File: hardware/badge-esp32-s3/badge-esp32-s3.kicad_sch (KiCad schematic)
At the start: 4 parts, among them U4 ESP32-S3-MINI-1-N8

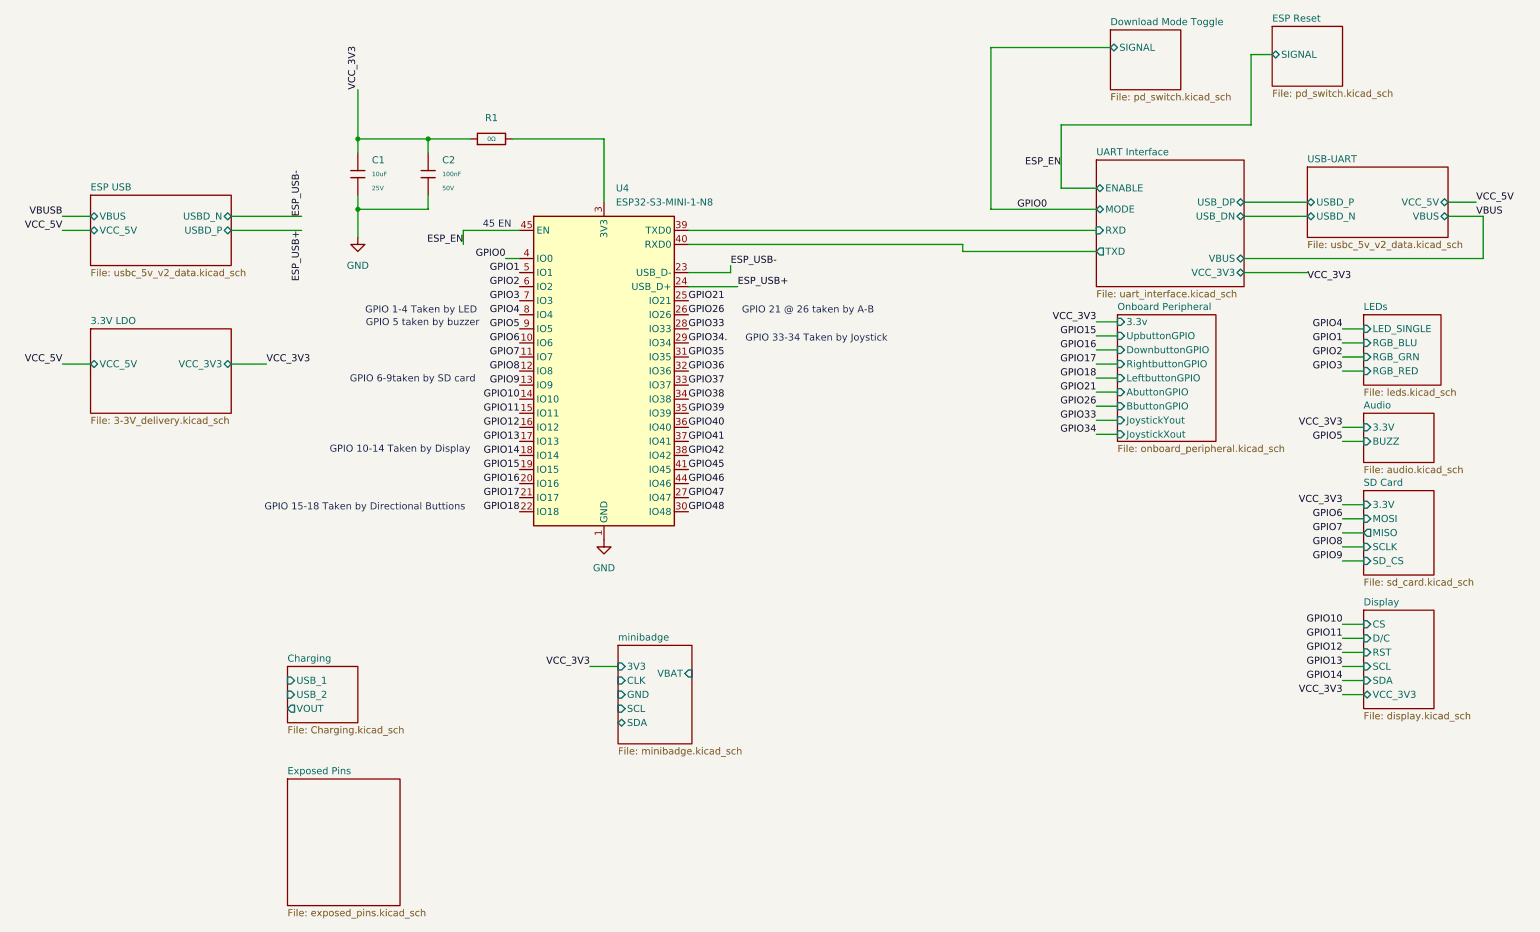
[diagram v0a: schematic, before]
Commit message: Fleshed out schematic with all exposed pins
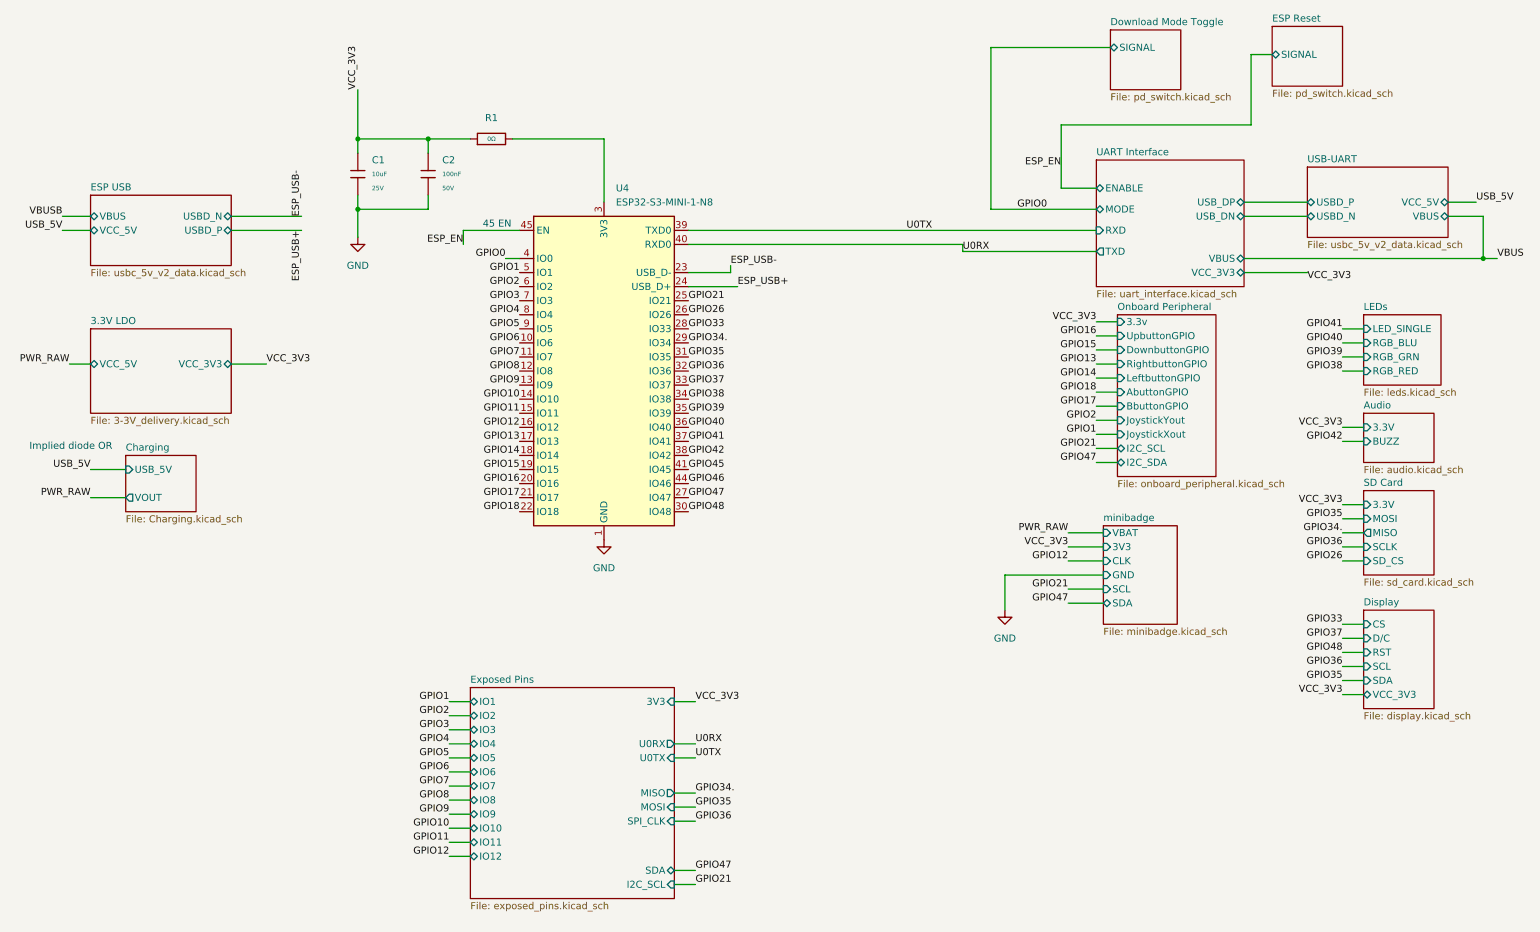
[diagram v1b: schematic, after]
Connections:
- net UART Interface/RXD renamed U0TX
- net UART Interface/TXD renamed U0RX
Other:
- sheet Charging ports: added USB_5V; removed USB_1, USB_2
- sheet Exposed Pins ports: added 3V3, I2C_SCL, IO1, IO10, IO11, IO12, IO2, IO3, IO4, IO5, IO6, IO7, IO8, IO9, MISO, MOSI, SDA, SPI_CLK, U0RX, U0TX; removed none
- sheet Onboard Peripheral ports: added I2C_SCL, I2C_SDA; removed none
- note added: "Implied diode OR"
- note removed: "GPIO 1-4 Taken by LED"
- note removed: "GPIO 10-14 Taken by Display"
- note removed: "GPIO 15-18 Taken by Directional Buttions"
- note removed: "GPIO 21 @ 26 taken by A-B"
- note removed: "GPIO 33-34 Taken by Joystick"
- note removed: "GPIO 5 taken by buzzer"
- note removed: "GPIO 6-9taken by SD card"

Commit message: Annotate schematic
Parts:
- renumbered U4 to U1
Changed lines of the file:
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@@
 		(dnp no)
 		(fields_autoplaced yes)
-		(property "Reference" "#PWR031"
+		(property "Reference" "#PWR02"
 			(at 118.11 114.3 0)
 			(effects
@@
 			(project ""
 				(path "/e2af9a6c-dbe9-4de2-9ba6-ea213a7300ec"
-					(reference "#PWR031")
+					(reference "#PWR02")
 					(unit 1)
 				)
@@
 		(dnp no)
 		(fields_autoplaced yes)
-		(property "Reference" "U4"
+		(property "Reference" "U1"
 			(at 120.2533 44.45 0)
 			(effects
@@
 			(project ""
 				(path "/e2af9a6c-dbe9-4de2-9ba6-ea213a7300ec"
-					(reference "U4")
+					(reference "U1")
 					(unit 1)
 				)
@@
 		(dnp no)
 		(fields_autoplaced yes)
-		(property "Reference" "#PWR047"
+		(property "Reference" "#PWR03"
 			(at 190.5 127 0)
 			(effects
@@
 			(project ""
 				(path "/e2af9a6c-dbe9-4de2-9ba6-ea213a7300ec"
-					(reference "#PWR047")
+					(reference "#PWR03")
 					(unit 1)
 				)
@@
 		(dnp no)
 		(fields_autoplaced yes)
-		(property "Reference" "#PWR021"
+		(property "Reference" "#PWR01"
 			(at 73.66 59.69 0)
 			(effects
@@
 			(project "badge-esp32-s3"
 				(path "/e2af9a6c-dbe9-4de2-9ba6-ea213a7300ec"
-					(reference "#PWR021")
+					(reference "#PWR01")
 					(unit 1)
 				)

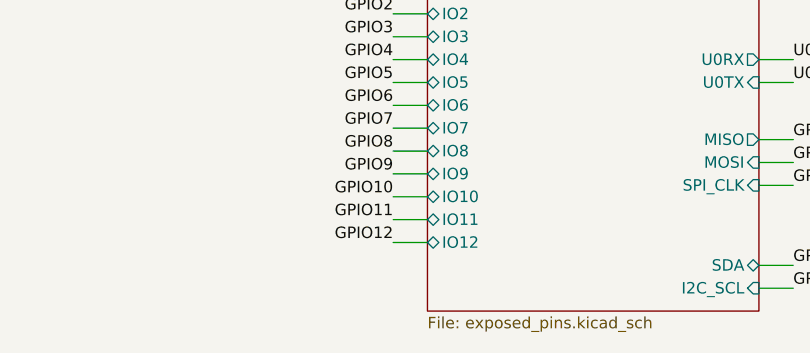
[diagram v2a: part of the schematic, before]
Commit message: Fix some DRC errors
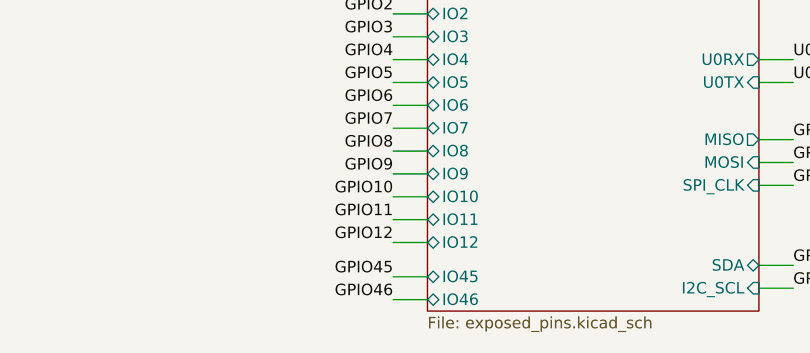
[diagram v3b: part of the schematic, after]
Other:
- sheet Exposed Pins ports: added IO45, IO46; removed none
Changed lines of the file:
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@@
+	(wire
+		(pts
+			(xy 90.17 168.91) (xy 93.98 168.91)
+		)
+		(stroke
+			(width 0)
+			(type default)
+		)
+	)
 	(wire
 		(pts
@@
 		(pts
 			(xy 238.76 20.32) (xy 234.95 20.32)
+		)
+		(stroke
+			(width 0)
+			(type default)
+		)
+	)
+	(wire
+		(pts
+			(xy 90.17 171.45) (xy 93.98 171.45)
 		)
 		(stroke
@@
 		)
 	)
+	(label "GPIO45"
+		(at 90.17 168.91 180)
+		(effects
+			(font
+				(size 1.27 1.27)
+			)
+			(justify right bottom)
+		)
+	)
 	(label "VCC_3V3"
 		(at 251.46 87.63 180)
@@
 	(label "GPIO6"
 		(at 102.87 72.39 180)
+		(effects
+			(font
+				(size 1.27 1.27)
+			)
+			(justify right bottom)
+		)
+	)
+	(label "GPIO46"
+		(at 90.17 171.45 180)
 		(effects
 			(font
@@
 			(effects
 				(font
+					(size 1.27 1.27)
+				)
+				(justify left)
+			)
+		)
+		(pin "IO45" bidirectional
+			(at 93.98 168.91 180)
+			(effects
+				(font
+					(size 1.27 1.27)
+				)
+				(justify left)
+			)
+		)
+		(pin "IO46" bidirectional
+			(at 93.98 171.45 180)
+			(effects
+				(font

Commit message: Finish schematic, start placing parts on layout
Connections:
- net VCC_3V3 renamed +3.3V
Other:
- sheet minibadge ports: added none; removed GND
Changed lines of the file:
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@@
 	)
 	(junction
+		(at 54.61 76.2)
+		(diameter 0)
+		(color 0 0 0 0)
+	)
+	(junction
 		(at 276.86 57.15)
 		(diameter 0)
@@
 	)
 	(junction
+		(at 26.67 100.33)
+		(diameter 0)
+		(color 0 0 0 0)
+	)
+	(junction
 		(at 73.66 48.26)
 		(diameter 0)
@@
 	(wire
 		(pts
+			(xy 26.67 109.22) (xy 26.67 100.33)
+		)
+		(stroke
+			(width 0)
+			(type default)
+		)
+	)
+	(wire
+		(pts
 			(xy 201.93 106.68) (xy 208.28 106.68)
 		)
@@
 	(wire
 		(pts
+			(xy 26.67 100.33) (xy 31.75 100.33)
+		)
+		(stroke
+			(width 0)
+			(type default)
+		)
+	)
+	(wire
+		(pts
 			(xy 251.46 109.22) (xy 255.27 109.22)
 		)
@@
 	(wire
 		(pts
-			(xy 73.66 48.26) (xy 73.66 53.34)
+			(xy 54.61 76.2) (xy 57.15 76.2)
 		)
 		(stroke
@@
 	(wire
 		(pts
-			(xy 251.46 74.93) (xy 255.27 74.93)
+			(xy 73.66 48.26) (xy 73.66 53.34)
 		)
 		(stroke
@@
 	(wire
 		(pts
-			(xy 190.5 114.3) (xy 190.5 120.65)
+			(xy 251.46 74.93) (xy 255.27 74.93)
 		)
 		(stroke
@@
 	(wire
 		(pts
-			(xy 86.36 35.56) (xy 86.36 38.1)
+			(xy 54.61 73.66) (xy 54.61 76.2)
 		)
 		(stroke
@@
 	(wire
 		(pts
-			(xy 90.17 147.32) (xy 93.98 147.32)
+			(xy 86.36 35.56) (xy 86.36 38.1)
 		)
 		(stroke
@@
 	(wire
 		(pts
-			(xy 90.17 154.94) (xy 93.98 154.94)
+			(xy 90.17 147.32) (xy 93.98 147.32)
 		)
 		(stroke
@@
 	(wire
 		(pts
-			(xy 73.66 35.56) (xy 73.66 38.1)
+			(xy 90.17 154.94) (xy 93.98 154.94)
 		)
 		(stroke
@@
 	(wire
 		(pts
-			(xy 251.46 90.17) (xy 255.27 90.17)
+			(xy 73.66 35.56) (xy 73.66 38.1)
 		)
 		(stroke
@@
 	(wire
 		(pts
-			(xy 208.28 114.3) (xy 190.5 114.3)
+			(xy 251.46 90.17) (xy 255.27 90.17)
 		)
 		(stroke
@@
 	(wire
 		(pts
-			(xy 25.4 100.33) (xy 31.75 100.33)
+			(xy 22.86 109.22) (xy 26.67 109.22)
 		)
 		(stroke
@@
 	(wire
 		(pts
-			(xy 50.8 76.2) (xy 57.15 76.2)
+			(xy 50.8 76.2) (xy 54.61 76.2)
 		)
 		(stroke
@@
 	(wire
 		(pts
+			(xy 15.24 100.33) (xy 26.67 100.33)
+		)
+		(stroke
+			(width 0)
+			(type default)
+		)
+	)
+	(wire
+		(pts
 			(xy 279.4 57.15) (xy 276.86 57.15)
 		)
@@
 	)
 	(label "PWR_RAW"
-		(at 25.4 100.33 180)
+		(at 22.86 109.22 180)
 		(effects
 			(font
@@
 		)
 	)
-	(label "VCC_3V3"
-		(at 73.66 26.67 90)
-		(effects
-			(font
-				(size 1.27 1.27)
-			)
-			(justify left bottom)
-		)
-	)
 	(label "GPIO48"
 		(at 251.46 128.27 180)
@@
 	)
 	(symbol
+		(lib_id "power:+3.3V")
+		(at 73.66 26.67 0)
+		(unit 1)
+		(exclude_from_sim no)
+		(in_bom yes)
+		(on_board yes)
+		(dnp no)
+		(fields_autoplaced yes)
+		(property "Reference" "#PWR068"
+			(at 73.66 30.48 0)
+			(effects
+				(font
+					(size 1.27 1.27)
+				)
+				(hide yes)
+			)
+		)
+		(property "Value" "+3.3V"
+			(at 73.66 21.59 0)
+			(effects
+				(font
+					(size 1.27 1.27)
+				)
+			)
+		)
+		(property "Footprint" ""
+			(at 73.66 26.67 0)
+			(effects
+				(font
+					(size 1.27 1.27)
+				)
+				(hide yes)
+			)
+		)
+		(property "Datasheet" ""
+			(at 73.66 26.67 0)
+			(effects
+				(font
+					(size 1.27 1.27)
+				)
+				(hide yes)
+			)
+		)
+		(property "Description" "Power symbol creates a global label with name \"+3.3V\""
+			(at 73.66 26.67 0)
+			(effects
+				(font
+					(size 1.27 1.27)
+				)
+				(hide yes)
+			)
+		)
+		(pin "1"
+		)
+		(instances
+			(project "badge-esp32-s3"
+				(path "/e2af9a6c-dbe9-4de2-9ba6-ea213a7300ec"
+					(reference "#PWR068")
+					(unit 1)
+				)
+			)
+		)
+	)
+	(symbol
 		(lib_id "PCM_JLCPCB-Capacitors:0603,100nF")
 		(at 86.36 41.91 0)
@@
 	)
 	(symbol
+		(lib_id "power:+4V")
+		(at 15.24 100.33 0)
+		(unit 1)
+		(exclude_from_sim no)
+		(in_bom yes)
+		(on_board yes)
+		(dnp no)
+		(fields_autoplaced yes)
+		(property "Reference" "#PWR067"
+			(at 15.24 104.14 0)
+			(effects
+				(font
+					(size 1.27 1.27)
+				)
+				(hide yes)
+			)
+		)
+		(property "Value" "+4V"
+			(at 15.24 95.25 0)
+			(effects
+				(font
+					(size 1.27 1.27)
+				)
+			)
+		)
+		(property "Footprint" ""
+			(at 15.24 100.33 0)
+			(effects
+				(font
+					(size 1.27 1.27)
+				)
+				(hide yes)
+			)
+		)
+		(property "Datasheet" ""
+			(at 15.24 100.33 0)
+			(effects
+				(font
+					(size 1.27 1.27)
+				)
+				(hide yes)
+			)
+		)
+		(property "Description" "Power symbol creates a global label with name \"+4V\""
+			(at 15.24 100.33 0)
+			(effects
+				(font
+					(size 1.27 1.27)
+				)
+				(hide yes)
+			)
+		)
+		(pin "1"
+		)
+		(instances
+			(project ""
+				(path "/e2af9a6c-dbe9-4de2-9ba6-ea213a7300ec"
+					(reference "#PWR067")
+					(unit 1)
+				)
+			)
+		)
+	)
+	(symbol
 		(lib_id "power:GND")
 		(at 118.11 107.95 0)
@@
 	)
 	(symbol
-		(lib_id "power:GND")
-		(at 190.5 120.65 0)
-		(unit 1)
-		(exclude_from_sim no)
-		(in_bom yes)
-		(on_board yes)
-		(dnp no)
-		(fields_autoplaced yes)
-		(property "Reference" "#PWR03"
-			(at 190.5 127 0)
-			(effects
-				(font
-					(size 1.27 1.27)
-				)
-				(hide yes)
-			)
-		)
-		(property "Value" "GND"
-			(at 190.5 125.73 0)
-			(effects
-				(font
-					(size 1.27 1.27)
-				)
-			)
-		)
-		(property "Footprint" ""
-			(at 190.5 120.65 0)
-			(effects
-				(font
-					(size 1.27 1.27)
-				)
-				(hide yes)
-			)
-		)
-		(property "Datasheet" ""
-			(at 190.5 120.65 0)
-			(effects
-				(font
-					(size 1.27 1.27)
-				)
-				(hide yes)
-			)
-		)
-		(property "Description" "Power symbol creates a global label with name \"GND\" , ground"
-			(at 190.5 120.65 0)
-			(effects
-				(font
-					(size 1.27 1.27)
-				)
-				(hide yes)
-			)
-		)
-		(pin "1"
-		)
-		(instances
-			(project ""
-				(path "/e2af9a6c-dbe9-4de2-9ba6-ea213a7300ec"
-					(reference "#PWR03")
-					(unit 1)
-				)
-			)
-		)
-	)
-	(symbol
 		(lib_id "PCM_JLCPCB-Capacitors:0603,10uF,(2)")
 		(at 73.66 41.91 0)
@@
 	)
 	(symbol
+		(lib_id "power:+3.3V")
+		(at 54.61 73.66 0)
+		(unit 1)
+		(exclude_from_sim no)
+		(in_bom yes)
+		(on_board yes)
+		(dnp no)
+		(fields_autoplaced yes)
+		(property "Reference" "#PWR03"
+			(at 54.61 77.47 0)
+			(effects
+				(font
+					(size 1.27 1.27)
+				)
+				(hide yes)
+			)
+		)
+		(property "Value" "+3.3V"
+			(at 54.61 68.58 0)
+			(effects
+				(font
+					(size 1.27 1.27)
+				)
+			)
+		)
+		(property "Footprint" ""
+			(at 54.61 73.66 0)
+			(effects
+				(font
+					(size 1.27 1.27)
+				)
+				(hide yes)
+			)
+		)
+		(property "Datasheet" ""
+			(at 54.61 73.66 0)
+			(effects
+				(font
+					(size 1.27 1.27)
+				)
+				(hide yes)
+			)
+		)
+		(property "Description" "Power symbol creates a global label with name \"+3.3V\""
+			(at 54.61 73.66 0)
+			(effects
+				(font
+					(size 1.27 1.27)
+				)
+				(hide yes)
+			)
+		)
+		(pin "1"
+		)
+		(instances
+			(project ""
+				(path "/e2af9a6c-dbe9-4de2-9ba6-ea213a7300ec"
+					(reference "#PWR03")
+					(unit 1)
+				)
+			)
+		)
+	)
+	(symbol
 		(lib_id "power:GND")
 		(at 73.66 53.34 0)
@@
 			(effects
 				(font
-					(size 1.27 1.27)
-				)
-				(justify left)
-			)
-		)
-		(pin "GND" input
-			(at 208.28 114.3 180)
-			(effects
-				(font
